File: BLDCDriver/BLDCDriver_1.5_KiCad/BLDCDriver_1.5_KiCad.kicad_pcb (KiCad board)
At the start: 2 copper layers, 42 x 43.2 mm, 70 parts, among them IC1 STSPIN32G4, J2 Debug, J3 Motor Out, J4 POWER, J5 CAN, SW1 SW_Push, U4 MCP2562-E-SN, U5 AS5048A-HTSP-500, U6 AP7375-33SA-7

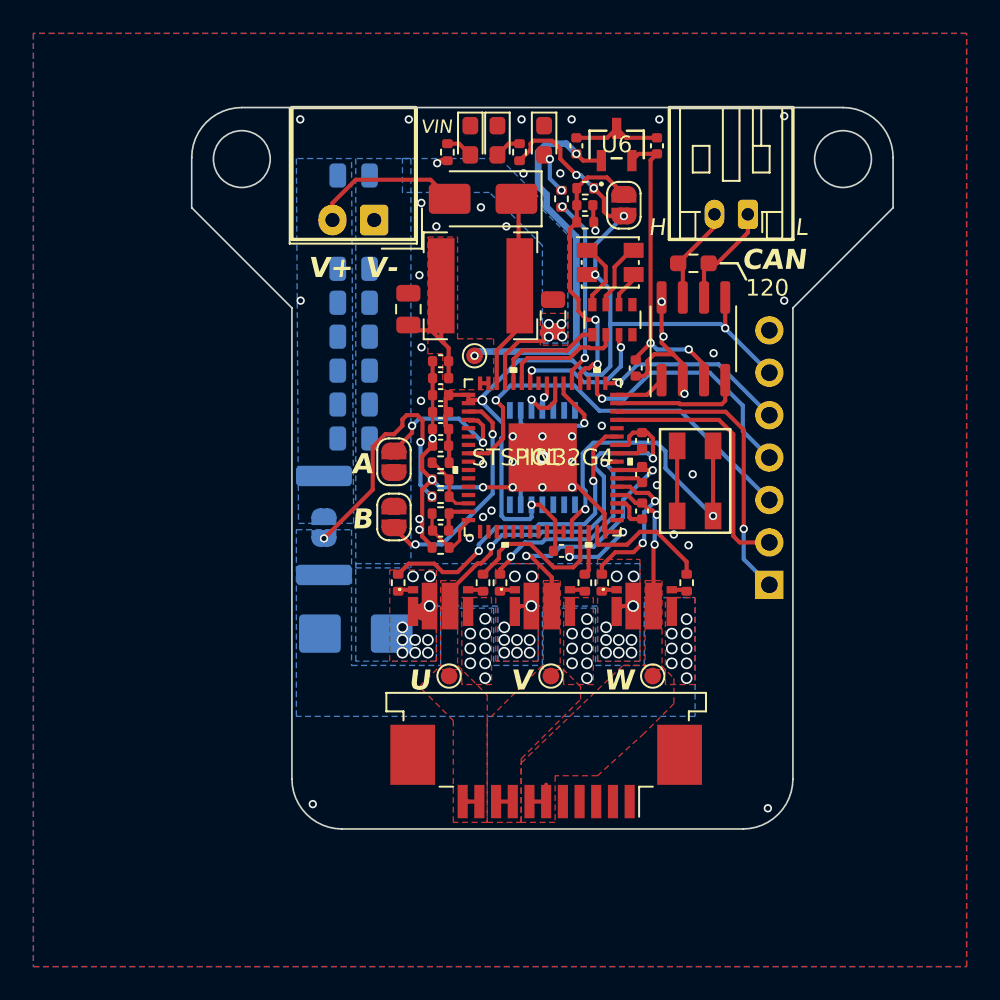
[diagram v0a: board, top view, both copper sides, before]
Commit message: ✨UARTで受信できる保険をかけた
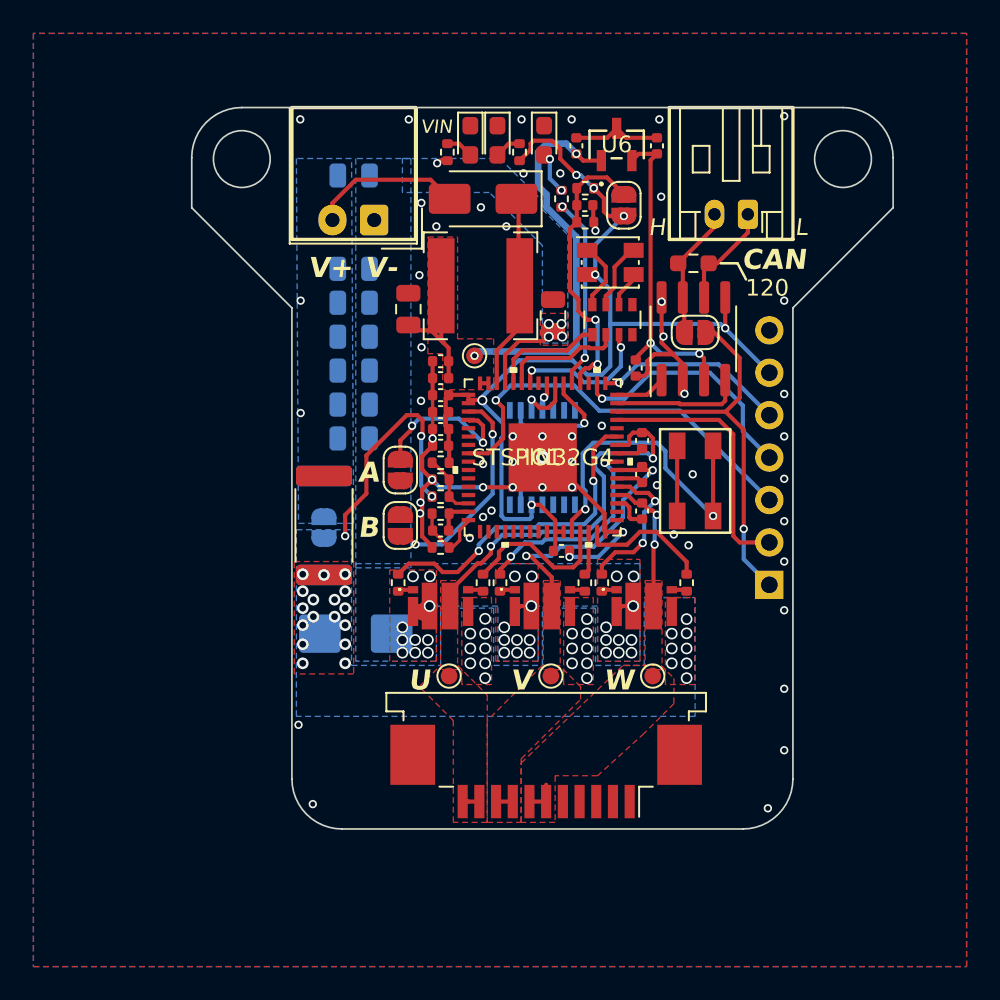
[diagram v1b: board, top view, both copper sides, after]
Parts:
- added JP5: Jumper_2_Open, Jumper:SolderJumper-2_P1.3mm_Open_RoundedPad1.0x1.5mm, F.Cu at (9.14, -7.49)
- added R19: 4mΩ, Resistor_SMD:R_2512_6332Metric, F.Cu at (-13.1, 4.06)
- C12: value N.M. -> 1uF
- D4: value LED_Green -> LED_Pink
- J3: value Motor Out -> FFC_11P_1mm
- U6: value AP7375-33SA-7 -> AP7375-50SA
- moved JP3 0.64 mm to (-8.51, 4.06)
- moved JP4 0.62 mm to (-8.51, 0.75)
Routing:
- net UART_RX: track 18.0 -> 25.3 mm
- net CANH: track 6.00 -> 8.13 mm
- net SHUNT_P1: track 15.7 -> 14.7 mm, vias 27 -> 44
- net SWA: track 13.6 -> 13.0 mm
- net GND: vias 49 -> 59
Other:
- board text added: "00 01 10 11"
- board text added: "1 2 3 4"
- board text added: "Designed By Daiki Tomioka"

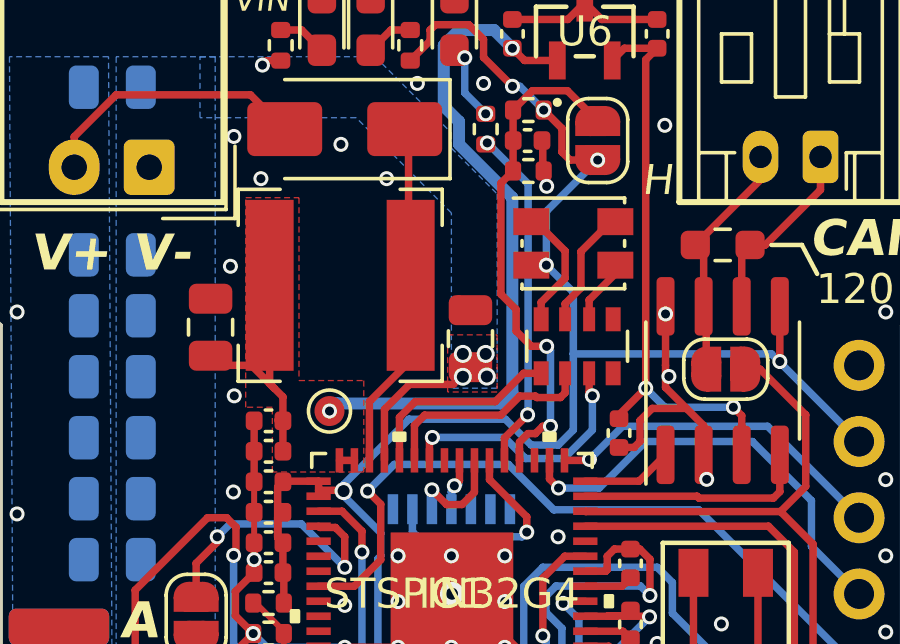
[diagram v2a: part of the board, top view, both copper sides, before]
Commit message: ⚠️PB8_BOOT0をGNDに落とした
データシート読まないと...
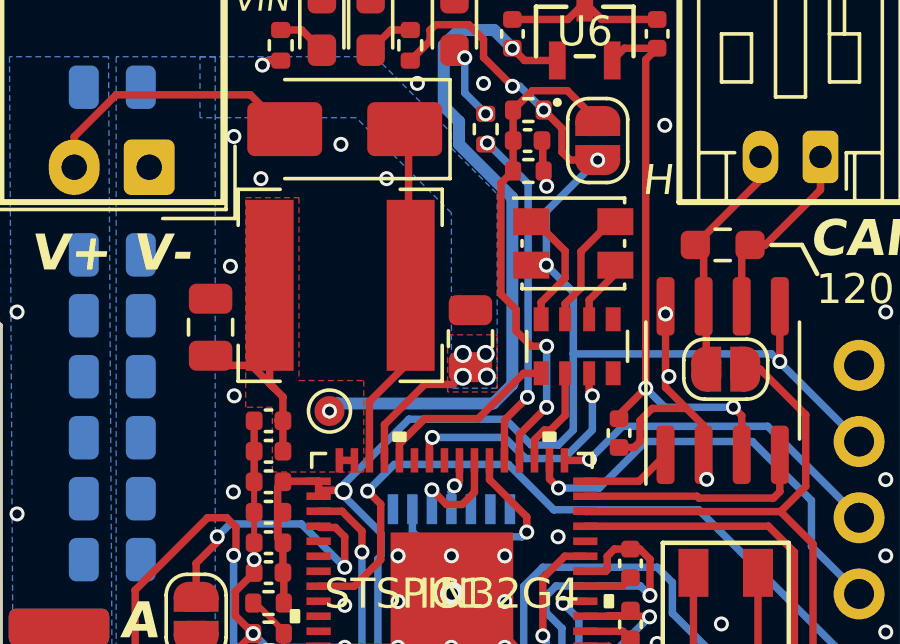
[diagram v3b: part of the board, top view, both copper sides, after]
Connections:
- IC1 pad 51: unconnected-(IC1-PA15-Pad51) -> LED_G
- IC1 pad 59: LED_G -> GND
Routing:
- net LED_G: track 7.33 -> 3.45 mm
- net LED_R: track 6.77 -> 6.25 mm
